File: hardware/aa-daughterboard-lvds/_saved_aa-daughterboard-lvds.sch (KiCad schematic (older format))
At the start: 107 parts, among them CN1 Barrel_Jack, CN10 6P6C, CN11 6P6C, CN12 6P6C, CN13 6P6C, CN14 Conn_01x08, CN15 Conn_01x08, CN16 Conn_01x08, CN17 8P8C, CN18 8P8C, CN19 8P8C, CN2 Conn_01x02, CN3 Conn_01x03, CN4 Conn_01x03, CN5 6P6C, CN6 Conn_01x04, CN7 Conn_01x04, CN8 Conn_01x04, CN9 Conn_01x04, P1 Conn_02x25_Odd_Even, P2 Conn_02x25_Odd_Even, Q1 TN1610H, U1 24LC08, U2 NIS5132xx, U3 uA7805, U4 75ALS192, U5 75ALS192, U6 75ALS192, U7 75ALS192, U8 75ALS192

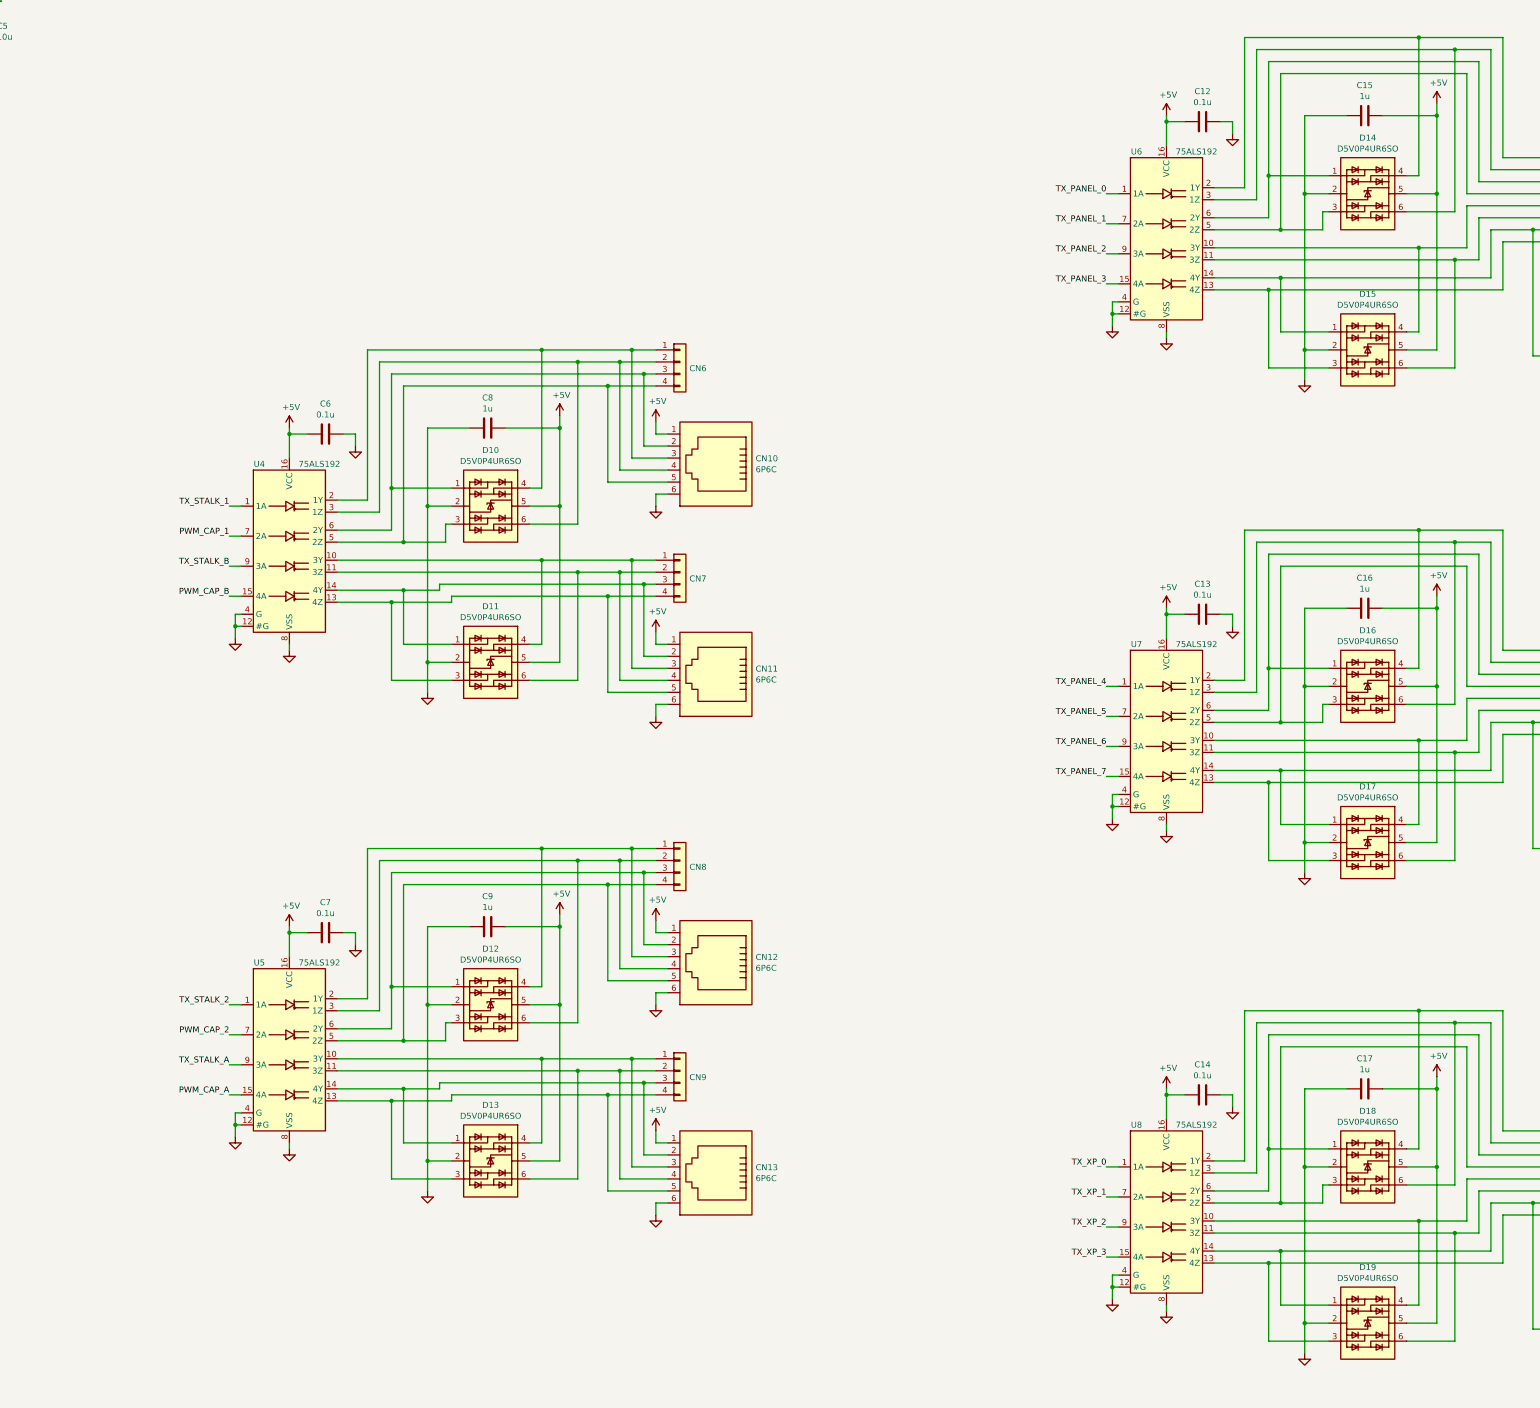
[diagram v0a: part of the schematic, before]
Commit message: Rough grouping of components done
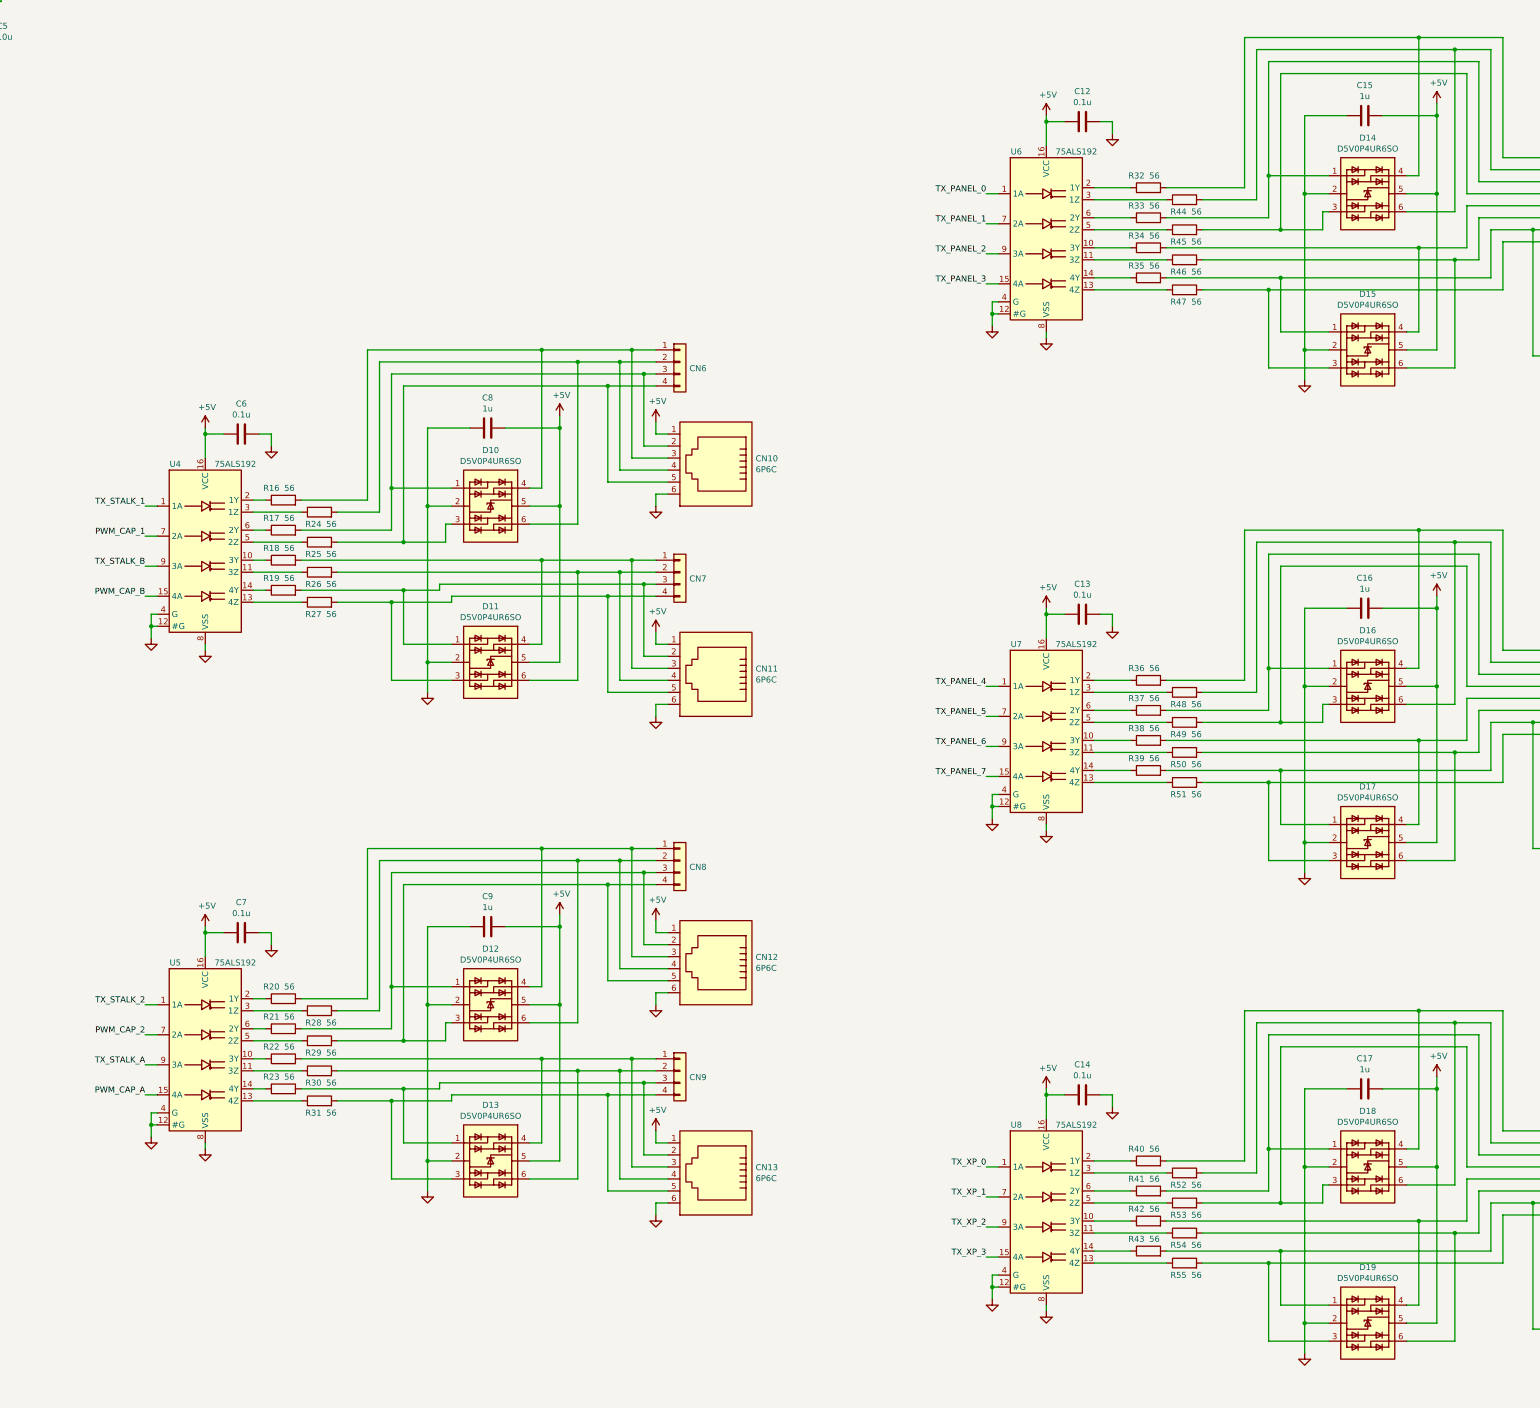
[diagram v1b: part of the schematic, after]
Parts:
- added R16, R17, R18, R19, R20, R21, R22, R23, R24, R25, R26, R27, R28, R29, R30, R31, R32, R33, R34, R35, R36, R37, R38, R39, R40, R41, R42, R43, R44, R45, R46, R47, R48, R49, R50, R51, R52, R53, R54, R55: 56, Resistor_SMD:R_0603_1608Metric, symbol Device:R
- Q1: footprint Package_TO_SOT_THT:TO-220-3_Horizontal_TabDown -> Package_TO_SOT_THT:TO-220-3_Vertical
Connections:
- wire segments 832 -> 872
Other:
- moved on the sheet: C12, C13, C14, C6, C7, U4, U5, U6, U7, U8
